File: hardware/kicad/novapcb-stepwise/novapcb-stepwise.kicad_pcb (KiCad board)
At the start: 6 copper layers, 90 x 70 mm, 129 parts, among them J1 USB-C_2.0, J10 CRSF_solder_pad, J11 ESC_solder_pad, J12 ESC_solder_pad, J13 ESC_solder_pad, J14 ESC_solder_pad, J15 ESC_solder_pad, J16 ESC_solder_pad, J17 ESC_solder_pad, J18 ESC_solder_pad, J19 MAUCH2_6P, J2 microSD_DM3AT, J20 CAN_4P, J3 TELEM_6P, J4 MAUCH_6P, J5 GPS_MAG_10P, J9 SWD_10P, Q2 AO3401A, Q3 AO4262E, Q4 AO4262E, Q5 AO3400A, U1 STM32H743VITx, U11 LM74700-Q1, U12 LM74700-Q1, U13 LP5907MFX-3.3, U14 TJA1051TK/3, U15 PESD2CAN, U2 AP2112K-3.3, U3 ICM-42688-P_LGA-14_2.5x3mm_P0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, U4 DPS310, U5 USBLC6-2P6, U6 TPS25940A, U7 LPS22HB, U8 BMI088, U9 LSM6DSV16X, Y1 8MHz

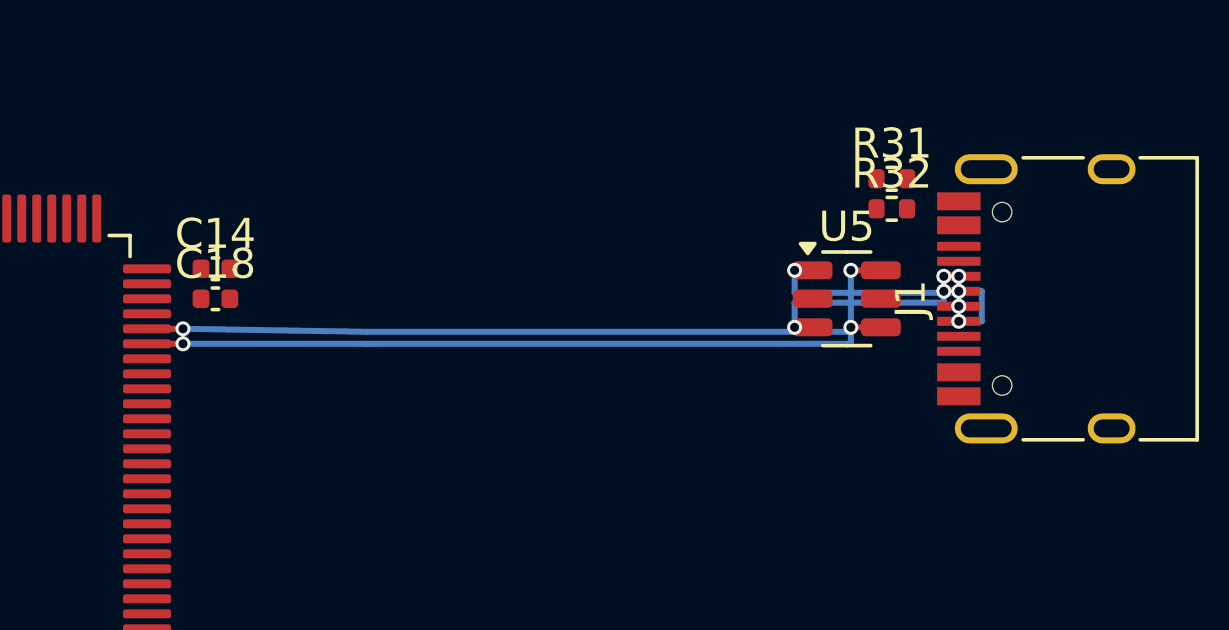
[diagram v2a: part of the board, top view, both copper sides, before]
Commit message: hw: C↔F WIP — bridges + Pair 1 Y fixed; openEMS coupled validation script
Per master 2026-05-22:
  - Bridge vias offset to X=81.0/82.5 (option b)
  - Pair 1 Y moved to 31.70/32.03 (south of Pair 2 vias at 30.95)
  - openEMS coupled-pair validation script started

Still WIP: routing hits U5's 6-pin tight grid (pads at 0.95mm pitch
incl. P5V at 77.14/30.00 which my v4_dpp at 77.30/29.80 conflicts
with). Pair 1 USB_DP at Y=31.70 B.Cu still crosses Pair 2 v3_dpp
B.Cu route — needs further reroute or topology change.

openEMS coupled-pair validation (val_openems_coupled.py): my
Garg-Bahl analytical implementation had a bug (negative ε_eff_odd);
deferred to a published-table cross-check. The 87.4Ω openEMS result
remains the working number; closed-form simple H-J + 0.48*exp formula
gives 99Ω (over-estimates because the 0.48*exp coupling factor is
valid only for S/h>1; our S/h=0.62 is moderate coupling where the
formula under-estimates the coupling magnitude). Will properly validate
in next iteration.

Asking master direction: the C↔F manual-routing iteration is consuming
significant cycles on geometric-tight conflicts. Recommend either:
  1. Use Freerouting on the USB nets specifically (designed for diff
     pair + via-around-obstacle problems)
  2. Re-place U5 with more space around it (currently 4×4mm body with
     pads 0.95mm apart blocks easy escape)
  3. Accept current routing state as v1 "best effort" pending later
     refinement

Co-Authored-By: Claude Opus 4.7 <noreply@anthropic.com>
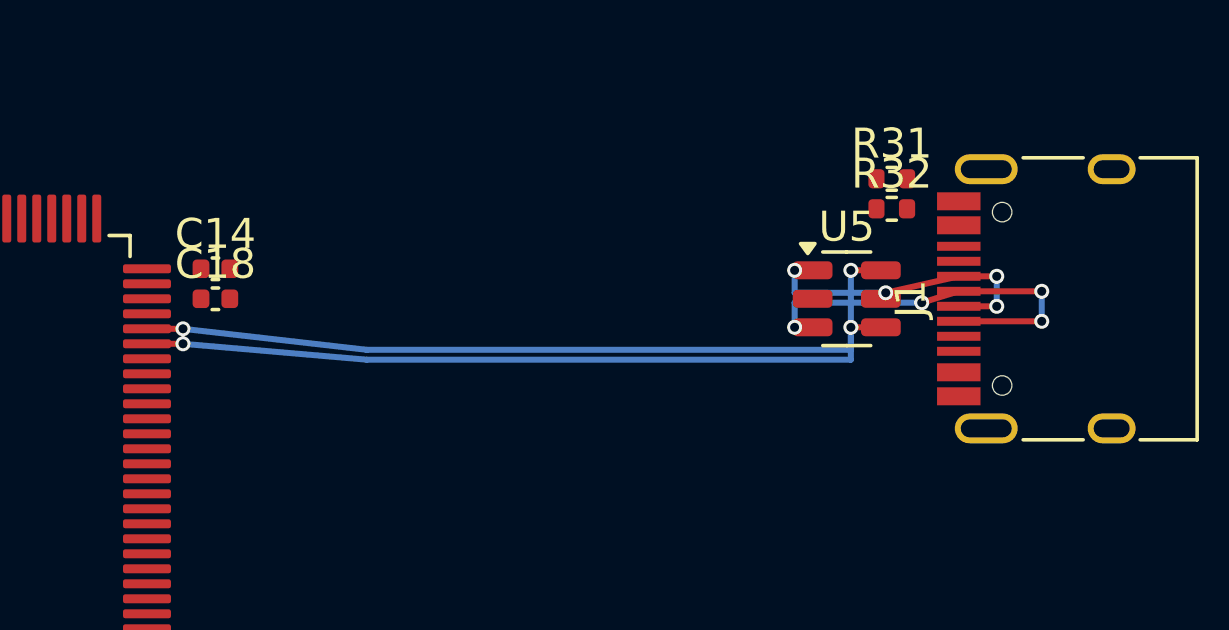
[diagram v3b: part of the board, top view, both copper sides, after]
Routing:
- net USBC_D_M_PRE: track 9.80 -> 13.5 mm
- net USBC_D_P_PRE: track 8.37 -> 10.4 mm
- net USB_DP: track 26.5 -> 27.2 mm
- net USB_DM: track 25.0 -> 25.6 mm
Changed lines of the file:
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@@
+	)
+	(segment
+		(start 78.5 30.13)
+		(end 79.735 29.75)
+		(width 0.2)
+		(layer "F.Cu")
+		(net 93)
+	)
+	(segment
+		(start 79.735 29.75)
+		(end 82.5 29.75)
+		(width 0.2)
+		(layer "F.Cu")
+		(net 93)
+	)
+	(segment
+		(start 82.5 30.75)
+		(end 79.735 30.75)
+		(width 0.2)
+		(layer "F.Cu")
+		(net 93)
 	)
 	(segment
@@
 		(net 93)
 	)
-	(segment
-		(start 79.235 29.75)
-		(end 79.735 29.75)
-		(width 0.2)
-		(layer "F.Cu")
+	(via
+		(at 78.5 30.13)
+		(size 0.5)
+		(drill 0.3)
+		(layers "F.Cu" "B.Cu")
 		(net 93)
 	)
@@
 	)
 	(via
-		(at 79.235 29.75)
-		(size 0.5)
-		(drill 0.3)
-		(layers "F.Cu" "B.Cu")
-		(net 93)
-	)
-	(via
-		(at 79.735 29.75)
-		(size 0.5)
-		(drill 0.3)
-		(layers "F.Cu" "B.Cu")
-		(net 93)
-	)
-	(via
-		(at 79.735 30.75)
-		(size 0.5)
-		(drill 0.3)
-		(layers "F.Cu" "B.Cu")
-		(net 93)
-	)
-	(segment
-		(start 79.235 30.13)
-		(end 79.235 29.75)
-		(width 0.2)
-		(layer "B.Cu")
+		(at 82.5 29.75)
+		(size 0.5)
+		(drill 0.3)
+		(layers "F.Cu" "B.Cu")
+		(net 93)
+	)
+	(via
+		(at 82.5 30.75)
+		(size 0.5)
+		(drill 0.3)
+		(layers "F.Cu" "B.Cu")
 		(net 93)
 	)
@@
 	)
 	(segment
-		(start 80.5 30.75)
-		(end 79.735 30.75)
-		(width 0.2)
-		(layer "B.Cu")
-		(net 93)
-	)
-	(segment
-		(start 80.5 29.75)
-		(end 80.5 30.75)
+		(start 82.5 29.75)
+		(end 82.5 30.75)
+		(width 0.2)
+		(layer "B.Cu")
+		(net 93)
+	)
+	(segment
+		(start 78.5 30.13)
+		(end 78.5 30.13)
 		(width 0.2)
 		(layer "B.Cu")
@@
 	(segment
 		(start 74.2625 30.13)
-		(end 79.235 30.13)
-		(width 0.2)
-		(layer "B.Cu")
-		(net 93)
-	)
-	(segment
-		(start 79.735 29.75)
-		(end 80.5 29.75)
-		(width 0.2)
-		(layer "B.Cu")
-		(net 93)
+		(end 78.5 30.13)
+		(width 0.2)
+		(layer "B.Cu")
+		(net 93)
+	)
+	(segment
+		(start 81 29.25)
+		(end 79.735 29.25)
+		(width 0.2)
+		(layer "F.Cu")
+		(net 94)
+	)
+	(segment
+		(start 77.3 29.8)
+		(end 79.735 29.25)
+		(width 0.2)
+		(layer "F.Cu")
+		(net 94)
 	)
 	(segment
@@
 	)
 	(segment
-		(start 79.235 29.25)
-		(end 79.735 29.25)
-		(width 0.2)
-		(layer "F.Cu")
+		(start 79.735 30.25)
+		(end 81 30.25)
+		(width 0.2)
+		(layer "F.Cu")
+		(net 94)
+	)
+	(via
+		(at 81 30.25)
+		(size 0.5)
+		(drill 0.3)
+		(layers "F.Cu" "B.Cu")
 		(net 94)
 	)
@@
 	)
 	(via
-		(at 79.735 29.25)
-		(size 0.5)
-		(drill 0.3)
-		(layers "F.Cu" "B.Cu")
-		(net 94)
-	)
-	(via
-		(at 79.235 29.25)
-		(size 0.5)
-		(drill 0.3)
-		(layers "F.Cu" "B.Cu")
-		(net 94)
-	)
-	(via
-		(at 79.735 30.25)
-		(size 0.5)
-		(drill 0.3)
-		(layers "F.Cu" "B.Cu")
+		(at 81 29.25)
+		(size 0.5)
+		(drill 0.3)
+		(layers "F.Cu" "B.Cu")
+		(net 94)
+	)
+	(via
+		(at 77.3 29.8)
+		(size 0.5)
+		(drill 0.3)
+		(layers "F.Cu" "B.Cu")
+		(net 94)
+	)
+	(segment
+		(start 81 30.25)
+		(end 81 29.25)
+		(width 0.2)
+		(layer "B.Cu")
+		(net 94)
+	)
+	(segment
+		(start 74.2625 29.8)
+		(end 77.3 29.8)
+		(width 0.2)
+		(layer "B.Cu")
+		(net 94)
+	)
+	(segment
+		(start 77.3 29.8)
+		(end 77.3 29.8)
+		(width 0.2)
+		(layer "B.Cu")
 		(net 94)
 	)
@@
 	)
 	(segment
-		(start 79.735 30.25)
-		(end 79.735 29.25)
-		(width 0.2)
-		(layer "B.Cu")
-		(net 94)
-	)
-	(segment
-		(start 79.235 29.8)
-		(end 79.235 29.25)
-		(width 0.2)
-		(layer "B.Cu")
-		(net 94)
-	)
-	(segment
-		(start 74.2625 29.8)
-		(end 79.235 29.8)
-		(width 0.2)
-		(layer "B.Cu")
-		(net 94)
+		(start 76.1375 30.95)
+		(end 77.1375 30.95)
+		(width 0.2)
+		(layer "F.Cu")
+		(net 95)
 	)
 	(segment
@@
 		(net 95)
 	)
-	(segment
-		(start 76.1375 30.95)
-		(end 77.1375 30.95)
-		(width 0.2)
-		(layer "F.Cu")
-		(net 95)
-	)
 	(via
 		(at 76.1375 30.95)
@@
 	)
 	(segment
-		(start 76.1375 31.5)
+		(start 60 32.03)
+		(end 76.1375 32.03)
+		(width 0.2)
+		(layer "B.Cu")
+		(net 95)
+	)
+	(segment
+		(start 76.1375 32.03)
 		(end 76.1375 30.95)
 		(width 0.2)
@@
 	)
 	(segment
-		(start 60 31.5)
-		(end 76.1375 31.5)
-		(width 0.2)
-		(layer "B.Cu")
-		(net 95)
-	)
-	(segment
 		(start 53.875 31.5)
-		(end 60 31.5)
+		(end 60 32.03)
 		(width 0.2)
 		(layer "B.Cu")
@@
 	)
 	(via
+		(at 53.875 31)
+		(size 0.5)
+		(drill 0.3)
+		(layers "F.Cu" "B.Cu")
+		(net 96)
+	)
+	(via
 		(at 76.1375 29.05)
 		(size 0.5)
@@
 		(net 96)
 	)
-	(via
-		(at 53.875 31)
-		(size 0.5)
-		(drill 0.3)
-		(layers "F.Cu" "B.Cu")
-		(net 96)
-	)
-	(segment
-		(start 76.1375 31.1)
+	(segment
+		(start 76.1375 31.7)
 		(end 76.1375 29.05)
 		(width 0.2)
@@
 	)
 	(segment
+		(start 60 31.7)
+		(end 76.1375 31.7)
+		(width 0.2)
+		(layer "B.Cu")
+		(net 96)
+	)
+	(segment
 		(start 53.875 31)
-		(end 60 31.1)
-		(width 0.2)
-		(layer "B.Cu")
-		(net 96)
-	)
-	(segment
-		(start 60 31.1)
-		(end 76.1375 31.1)
-		(width 0.2)
-		(layer "B.Cu")
+		(end 60 31.7)
+		(width 0.2)
+		(layer "B.Cu")

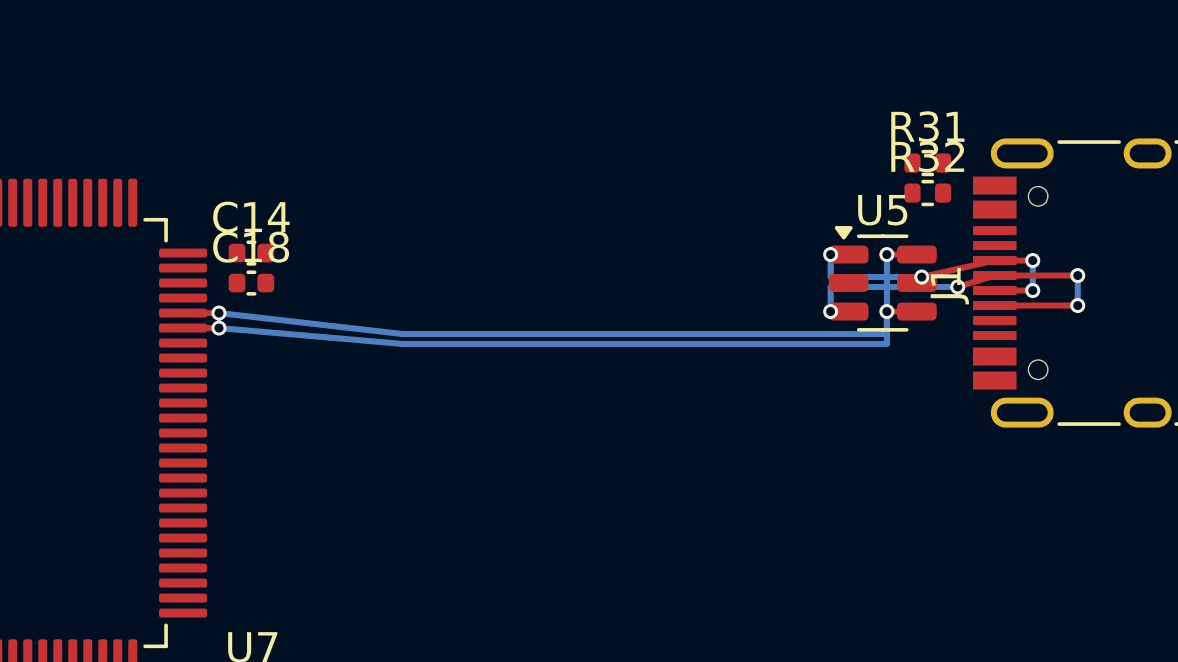
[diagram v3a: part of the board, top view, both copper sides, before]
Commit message: proc+hw: ENGINEERING_RIGOR §7 root-cause discipline; RF-3 stale-docs; F replace
Per Sai 2026-05-23 root-cause directive + master 2026-05-23 hard-review.

## ENGINEERING_RIGOR §7 (NEW)

Adds the root-cause discipline rule: every fix PR/commit must state
(1) root cause traced to origin, (2) root vs stopgap, (3) if stopgap
— why now, logged to OPEN_QUESTIONS for follow-up. Patch-instinct
list ("omit the feature", "accept with known violations", "defer to
v2", "nudge one number"). Three worked examples from recent history.

Root cause of this rule's necessity: the analytical-H-J → openEMS
Z_diff finding (70Ω vs 94Ω) — if we had shipped on the analytical
"floor", USB-2 would have been out of spec. Sai's directive caught
the pattern: patches accumulate, root-fix is durable.

## RF-3 doc hygiene

- OPEN_QUESTIONS phase0.6-2 (openEMS Z0-extraction broken): marked
  RESOLVED 2026-05-22; Task 9 + the 3 traps captured.
- OPEN_QUESTIONS phase3exit-can (CAN excluded for v1): marked
  RE-OPENED — v1.1 ships 1× CAN per commit 13d26a8 (R1.4).

## Step-3 F re-placement (root fix)

step3_place_F.py: U5 moved (76, 30)→(76, 35) — out of the diff-pair
Y=31 corridor. F zone Y extended from 42→45 (borrows from G's
allocation; SUBSYSTEM_CONTRACTS update pending). Root cause of the
C↔F routing whack-a-mole: over-constrained region — U5 IN the pair's
Y-corridor. Not a router problem; placement.

integ_C_F.py: re-route attempt with new placement. PAIR 1 still has
1 DRC violation: DM vertical at X=78 physically intersects DP
horizontal at Y=34.05 (genuine geometric collision — the south-fan
topology needs both traces' Y-rows to be DIFFERENT for parallel
verticals, and the post-fan horizontal of DP crosses DM's vertical).

Root fix in flight: redesign the south-fan as coupled-diagonal +
parallel-vertical so both pair members descend together without
crossing. Working iteration.

Renders + .kicad_pcb attached (current WIP state).

Co-Authored-By: Claude Opus 4.7 <noreply@anthropic.com>
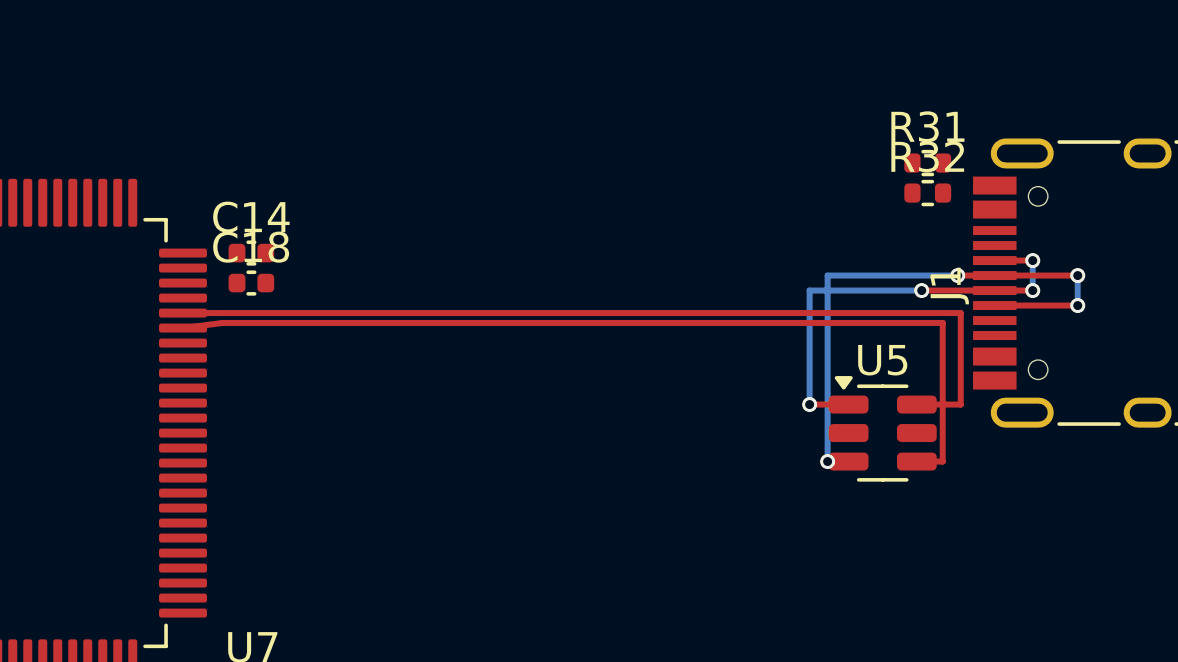
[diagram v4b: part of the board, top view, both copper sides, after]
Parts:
- moved U5 5.00 mm to (76.0, 35.0)
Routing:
- net USBC_D_M_PRE: track 13.5 -> 19.0 mm
- net USB_DM: track 25.6 -> 30.8 mm, vias 2 -> 0
- net USBC_D_P_PRE: track 10.4 -> 14.8 mm
- net USB_DP: track 27.2 -> 30.4 mm, vias 2 -> 0
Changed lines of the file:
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@@
 	(footprint "Package_TO_SOT_SMD:SOT-23-6"
 		(layer "F.Cu")
-		(at 76 30)
+		(at 76 35)
 		(descr "SOT, 6 Pin (JEDEC MO-178 Var AB https://www.jedec.org/document_search?search_api_views_fulltext=MO-178), generated with kicad-footprint-generator ipc_gullwing_generator.py")
 		(tags "SOT TO_SOT_SMD")
@@
 	)
 	(segment
-		(start 78.5 30.13)
+		(start 74.8625 35.95)
+		(end 74.1625 35.95)
+		(width 0.2)
+		(layer "F.Cu")
+		(net 93)
+	)
+	(segment
+		(start 82.5 30.75)
+		(end 79.735 30.75)
+		(width 0.2)
+		(layer "F.Cu")
+		(net 93)
+	)
+	(segment
+		(start 78.5 29.75)
 		(end 79.735 29.75)
 		(width 0.2)
@@
 		(width 0.2)
 		(layer "F.Cu")
-		(net 93)
-	)
-	(segment
-		(start 82.5 30.75)
-		(end 79.735 30.75)
-		(width 0.2)
-		(layer "F.Cu")
-		(net 93)
-	)
-	(segment
-		(start 74.8625 30.95)
-		(end 74.2625 30.95)
-		(width 0.2)
-		(layer "F.Cu")
-		(net 93)
-	)
-	(via
-		(at 78.5 30.13)
-		(size 0.5)
-		(drill 0.3)
-		(layers "F.Cu" "B.Cu")
-		(net 93)
-	)
-	(via
-		(at 74.2625 30.95)
-		(size 0.5)
-		(drill 0.3)
-		(layers "F.Cu" "B.Cu")
 		(net 93)
 	)
@@
 	)
 	(via
+		(at 74.1625 35.95)
+		(size 0.5)
+		(drill 0.3)
+		(layers "F.Cu" "B.Cu")
+		(net 93)
+	)
+	(via
 		(at 82.5 30.75)
 		(size 0.5)
@@
 		(net 93)
 	)
-	(segment
-		(start 74.2625 30.95)
-		(end 74.2625 30.13)
+	(via
+		(at 78.5 29.75)
+		(size 0.5)
+		(drill 0.3)
+		(layers "F.Cu" "B.Cu")
+		(net 93)
+	)
+	(segment
+		(start 74.1625 29.75)
+		(end 78.5 29.75)
 		(width 0.2)
 		(layer "B.Cu")
@@
 	)
 	(segment
-		(start 78.5 30.13)
-		(end 78.5 30.13)
+		(start 74.1625 35.95)
+		(end 74.1625 29.75)
 		(width 0.2)
 		(layer "B.Cu")
@@
 	)
 	(segment
-		(start 74.2625 30.13)
-		(end 78.5 30.13)
+		(start 77.3 30.25)
+		(end 79.735 30.25)
 		(width 0.2)
-		(layer "B.Cu")
-		(net 93)
+		(layer "F.Cu")
+		(net 94)
 	)
 	(segment
@@
 	)
 	(segment
-		(start 77.3 29.8)
-		(end 79.735 29.25)
-		(width 0.2)
-		(layer "F.Cu")
-		(net 94)
-	)
-	(segment
-		(start 74.8625 29.05)
-		(end 74.2625 29.05)
-		(width 0.2)
-		(layer "F.Cu")
-		(net 94)
-	)
-	(segment
 		(start 79.735 30.25)
 		(end 81 30.25)
 		(width 0.2)
 		(layer "F.Cu")
+		(net 94)
+	)
+	(segment
+		(start 74.8625 34.05)
+		(end 73.5625 34.05)
+		(width 0.2)
+		(layer "F.Cu")
+		(net 94)
+	)
+	(via
+		(at 73.5625 34.05)
+		(size 0.5)
+		(drill 0.3)
+		(layers "F.Cu" "B.Cu")
+		(net 94)
+	)
+	(via
+		(at 77.3 30.25)
+		(size 0.5)
+		(drill 0.3)
+		(layers "F.Cu" "B.Cu")
 		(net 94)
 	)
@@
 	)
 	(via
-		(at 74.2625 29.05)
-		(size 0.5)
-		(drill 0.3)
-		(layers "F.Cu" "B.Cu")
-		(net 94)
-	)
-	(via
 		(at 81 29.25)
 		(size 0.5)
@@
 		(net 94)
 	)
-	(via
-		(at 77.3 29.8)
-		(size 0.5)
-		(drill 0.3)
-		(layers "F.Cu" "B.Cu")
-		(net 94)
-	)
 	(segment
 		(start 81 30.25)
@@
 	)
 	(segment
-		(start 74.2625 29.8)
-		(end 77.3 29.8)
+		(start 73.5625 30.25)
+		(end 77.3 30.25)
 		(width 0.2)
 		(layer "B.Cu")
@@
 	)
 	(segment
-		(start 77.3 29.8)
-		(end 77.3 29.8)
+		(start 73.5625 34.05)
+		(end 73.5625 30.25)
 		(width 0.2)
 		(layer "B.Cu")
@@
 	)
 	(segment
-		(start 74.2625 29.05)
-		(end 74.2625 29.8)
+		(start 78 35.95)
+		(end 77.1375 35.95)
 		(width 0.2)
-		(layer "B.Cu")
-		(net 94)
-	)
-	(segment
-		(start 76.1375 30.95)
-		(end 77.1375 30.95)
+		(layer "F.Cu")
+		(net 95)
+	)
+	(segment
+		(start 52.675 31.5)
+		(end 54 31.33)
 		(width 0.2)
 		(layer "F.Cu")
@@
 	)
 	(segment
-		(start 52.675 31.5)
-		(end 53.875 31.5)
+		(start 78 31.33)
+		(end 78 35.95)
 		(width 0.2)
 		(layer "F.Cu")
 		(net 95)
 	)
-	(via
-		(at 76.1375 30.95)
-		(size 0.5)
-		(drill 0.3)
-		(layers "F.Cu" "B.Cu")
+	(segment
+		(start 54 31.33)
+		(end 78 31.33)
+		(width 0.2)
+		(layer "F.Cu")
 		(net 95)
 	)
-	(via
-		(at 53.875 31.5)
-		(size 0.5)
-		(drill 0.3)
-		(layers "F.Cu" "B.Cu")
-		(net 95)
-	)
-	(segment
-		(start 60 32.03)
-		(end 76.1375 32.03)
+	(segment
+		(start 52.675 31)
+		(end 54 31)
 		(width 0.2)
-		(layer "B.Cu")
-		(net 95)
-	)
-	(segment
-		(start 76.1375 32.03)
-		(end 76.1375 30.95)
+		(layer "F.Cu")
+		(net 96)
+	)
+	(segment
+		(start 78.6 34.05)
+		(end 77.1375 34.05)
 		(width 0.2)
-		(layer "B.Cu")
-		(net 95)
-	)
-	(segment
-		(start 53.875 31.5)
-		(end 60 32.03)
+		(layer "F.Cu")
+		(net 96)
+	)
+	(segment
+		(start 78.6 31)
+		(end 78.6 34.05)
 		(width 0.2)
-		(layer "B.Cu")
-		(net 95)
-	)
-	(segment
-		(start 52.675 31)
-		(end 53.875 31)
+		(layer "F.Cu")
+		(net 96)
+	)
+	(segment
+		(start 54 31)
+		(end 78.6 31)
 		(width 0.2)
 		(layer "F.Cu")
 		(net 96)
 	)
-	(segment
-		(start 76.1375 29.05)
-		(end 77.1375 29.05)
-		(width 0.2)
-		(layer "F.Cu")
-		(net 96)
-	)
-	(via
-		(at 53.875 31)
-		(size 0.5)
-		(drill 0.3)
-		(layers "F.Cu" "B.Cu")
-		(net 96)
-	)
-	(via
-		(at 76.1375 29.05)
-		(size 0.5)
-		(drill 0.3)
-		(layers "F.Cu" "B.Cu")
-		(net 96)
-	)
-	(segment
-		(start 76.1375 31.7)
-		(end 76.1375 29.05)
-		(width 0.2)
-		(layer "B.Cu")
-		(net 96)
-	)
-	(segment
-		(start 60 31.7)
-		(end 76.1375 31.7)
-		(width 0.2)
-		(layer "B.Cu")
-		(net 96)
-	)
-	(segment
-		(start 53.875 31)
-		(end 60 31.7)
-		(width 0.2)
-		(layer "B.Cu")
-		(net 96)
-	)
